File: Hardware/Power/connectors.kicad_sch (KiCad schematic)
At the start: 3 parts, among them J1 Conn_02x23_Odd_Even, J2 Screw_Terminal_01x03, J3 Conn_02x23_Odd_Even

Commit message: schematic update & pcb update
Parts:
- removed J1: Conn_02x23_Odd_Even, PLC_STM_Power:PRT12790, symbol Connector_Generic:Conn_02x23_Odd_Even
- removed J2: Screw_Terminal_01x03, PLC_STM_Power:TBC05031GG, symbol Connector:Screw_Terminal_01x03
- added J1: POWER, PLC_STM:1725656, symbol Connector:Screw_Terminal_01x02
- added J2: NUCLEO LEFT, PLC_STM_Power:PRT12790, symbol Connector_Generic:Conn_02x23_Odd_Even
- J3: value Conn_02x23_Odd_Even -> NUCLEO RIGHT
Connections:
- net +24V: now also J1.2 (Pin_2)
- net GND: now also J3.27 (Pin_27), J3.39 (Pin_39), J3.8 (Pin_8), J1.1 (Pin_1), J2.11 (Pin_11), J2.13 (Pin_13), J2.30 (Pin_30), J2.39 (Pin_39)
- net UART6_TX: now reaches J3.1 (Pin_1)
- net UART6_TX: now also J3.11 (Pin_11), J3.40 (Pin_40)
- net AO1: now reaches J3.10 (Pin_10)
- net ANALOG_IN6: now reaches J3.12 (Pin_12)
- net CAN2_RX: now reaches J3.13 (Pin_13)
- net CAN2_RX: now also J3.7 (Pin_7)
- net ANALOG_IN7: now reaches J3.14 (Pin_14)
- net AI0: now reaches J3.17 (Pin_17)
- net CAN1_RX: now reaches J3.2 (Pin_2)
- net CAN1_RX: now also J2.41 (Pin_41)
- net AVDD: now reaches J3.23 (Pin_23)
- net AVDD: now also J3.6 (Pin_6)
- net AGND: now reaches J3.25 (Pin_25)
- net CAN1_TX: now reaches J3.4 (Pin_4)
- net CAN1_TX: now also J2.43 (Pin_43)
- net UART6_RX: now reaches J3.42 (Pin_42)
- net UART5_TX: now reaches J3.44 (Pin_44)
- net UART5_TX: now also J2.10 (Pin_10)
- net UART5_RX: now reaches J3.46 (Pin_46)
- net UART5_RX: now also J2.12 (Pin_12)
- net CAN2_TX: now reaches J3.5 (Pin_5)
- new net 3V3: J2.7 (Pin_7)
- new net 5V: J2.9 (Pin_9)
- new net ANALOG_IN10: J2.21 (Pin_21)
- new net ANALOG_IN13: J2.23 (Pin_23)
- new net ANALOG_IN3: J2.19 (Pin_19)
- new net ANALOG_IN3/15: J2.27 (Pin_27)
- new net ANALOG_IN3/5: J2.42 (Pin_42)
- new net ANALOG_IN3/6: J2.40 (Pin_40)
- new net ANALOG_IN3/7: J2.44 (Pin_44)
- new net ANALOG_IN3/8: J2.29 (Pin_29)
- new net ANALOG_IN3/9: J2.25 (Pin_25)
- new net UART2_RX: J2.22 (Pin_22)
- new net UART2_TX: J2.24 (Pin_24)
- new net UART4_RX: J2.8 (Pin_8)
- new net UART4_TX: J2.6 (Pin_6)
- new net VIN: J2.15 (Pin_15)
- no-connect marks 1 -> 51
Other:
- moved on the sheet: J3

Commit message: schematic update & pcb update
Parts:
- J2, J3: footprint PLC_STM_Power:PRT12790 -> PLC_STM:PRT12790
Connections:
- net VIN is gone; now on net +5V: J2.15 (Pin_15)
- net +15V: now reaches J3.21 (Pin_21)
- net -15V: now reaches J2.18 (Pin_18)
- net 3V3 renamed +3V3
- net 5V renamed +5V
- net AI0 renamed AO_0
- net ANALOG_IN10: no longer names the net of J2.21 (Pin_21)
- net ANALOG_IN13: no longer names the net of J2.23 (Pin_23)
- net ANALOG_IN3: no longer names the net of J2.19 (Pin_19)
- net ANALOG_IN3/15: no longer names the net of J2.27 (Pin_27)
- net ANALOG_IN3/5: no longer names the net of J2.42 (Pin_42)
- net ANALOG_IN3/6: no longer names the net of J2.40 (Pin_40)
- net ANALOG_IN3/7: no longer names the net of J2.44 (Pin_44)
- net ANALOG_IN3/8: no longer names the net of J2.29 (Pin_29)
- net ANALOG_IN3/9: no longer names the net of J2.25 (Pin_25)
- net AO1 renamed AO_1
- no-connect marks 51 -> 56

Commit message: digital output & power finished
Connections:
- net UART2_RX is gone; now on net GND: J2.22 (Pin_22)
- net +15V: now also J2.10 (Pin_10); no longer J3.21 (Pin_21)
- net +24V: now also J2.29 (Pin_29); no longer J1.2 (Pin_2)
- net +3V3: now also J2.25 (Pin_25); no longer J2.7 (Pin_7)
- net +5V: now also J2.27 (Pin_27); no longer J2.15 (Pin_15), J2.9 (Pin_9)
- net -15V: now also J2.26 (Pin_26); no longer J2.18 (Pin_18)
- net GND: now also J2.19 (Pin_19), J2.20 (Pin_20), J3.20 (Pin_20); no longer J2.11 (Pin_11), J2.13 (Pin_13), J2.30 (Pin_30), J2.39 (Pin_39), J3.27 (Pin_27), J3.8 (Pin_8)
- net AGND: no longer names the net of J3.25 (Pin_25)
- net ANALOG_IN6: no longer names the net of J3.12 (Pin_12)
- net ANALOG_IN7: no longer names the net of J3.14 (Pin_14)
- net AO_0: no longer names the net of J3.17 (Pin_17)
- net AO_1: no longer names the net of J3.10 (Pin_10)
- net AVDD: no longer names the net of J3.23 (Pin_23)
- net AVDD: no longer J3.6 (Pin_6)
- net CAN1_RX: no longer names the net of J3.2 (Pin_2)
- net CAN1_RX: no longer J2.41 (Pin_41)
- net CAN1_TX: no longer names the net of J3.4 (Pin_4)
- net CAN1_TX: no longer J2.43 (Pin_43)
- net CAN2_RX: no longer names the net of J3.13 (Pin_13)
- net CAN2_RX: no longer J3.7 (Pin_7)
- net CAN2_TX: no longer names the net of J3.5 (Pin_5)
- net UART2_TX: no longer names the net of J2.24 (Pin_24)
- net UART4_RX: no longer names the net of J2.8 (Pin_8)
- net UART4_TX: no longer names the net of J2.6 (Pin_6)
- net UART5_RX: no longer names the net of J3.46 (Pin_46)
- net UART5_RX: no longer J2.12 (Pin_12)
- net UART5_TX: no longer names the net of J3.44 (Pin_44)
- net UART5_TX: no longer J2.10 (Pin_10)
- net UART6_RX: no longer names the net of J3.42 (Pin_42)
- removed net UART6_TX: J3.1 (Pin_1), J3.11 (Pin_11), J3.40 (Pin_40)
- new net VCC: J1.2 (Pin_2)
- no-connect marks 56 -> 82

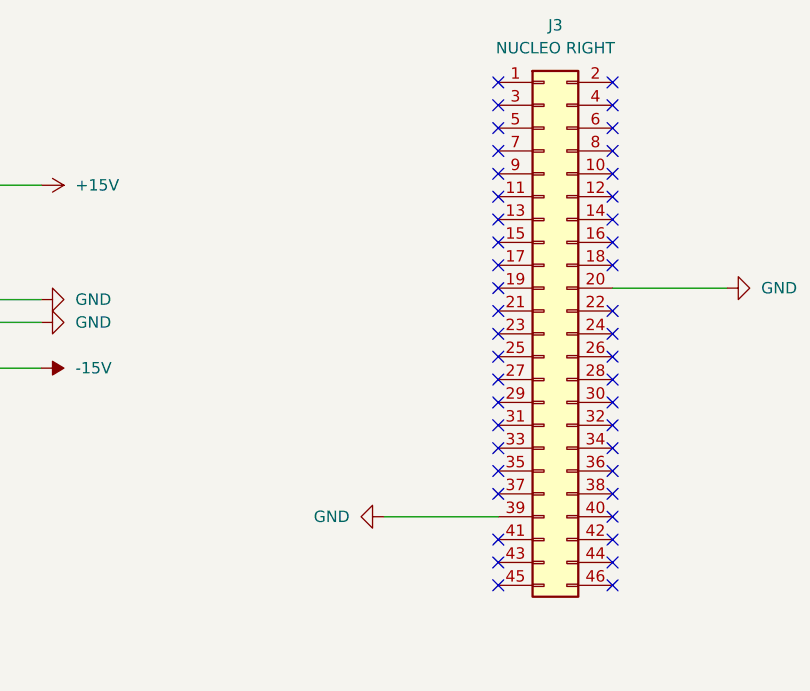
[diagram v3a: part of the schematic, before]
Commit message: analog & can finished
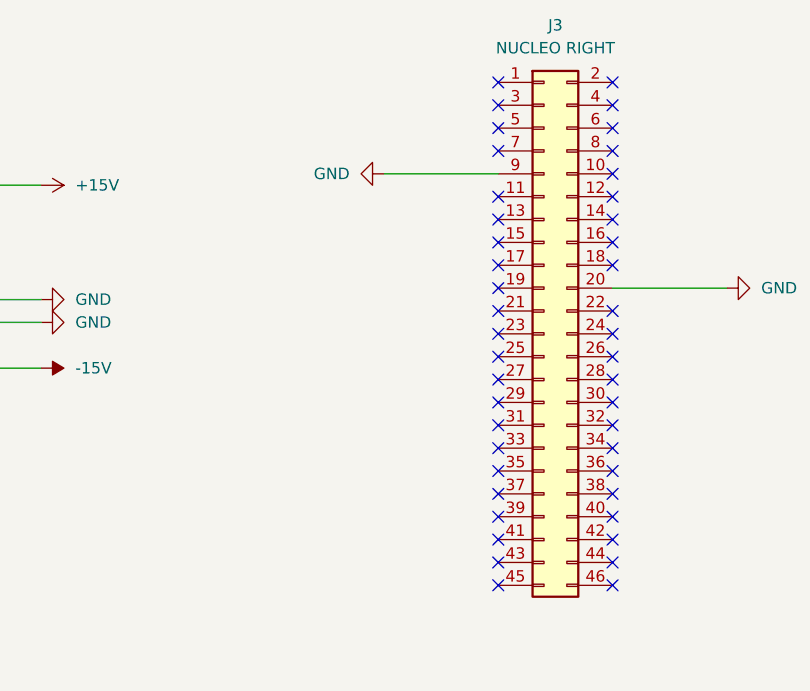
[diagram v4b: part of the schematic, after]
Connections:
- net GND: now also J3.9 (Pin_9); no longer J3.39 (Pin_39)
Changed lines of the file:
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@@
-	)
-	(no_connect
-		(at 217.17 78.74)
 	)
 	(no_connect
@@
 	)
 	(no_connect
+		(at 217.17 116.84)
+	)
+	(no_connect
 		(at 153.67 115.57)
 	)
@@
 	(wire
 		(pts
-			(xy 217.17 116.84) (xy 204.47 116.84)
+			(xy 217.17 78.74) (xy 204.47 78.74)
 		)
 		(stroke
@@
 	(symbol
 		(lib_id "power:GND")
-		(at 204.47 116.84 270)
+		(at 204.47 78.74 270)
 		(mirror x)
 		(unit 1)
@@
 		(fields_autoplaced yes)
 		(property "Reference" "#PWR025"
-			(at 198.12 116.84 0)
+			(at 198.12 78.74 0)
 			(effects
 				(font
@@
 		)
 		(property "Value" "GND"
-			(at 200.66 116.8399 90)
+			(at 200.66 78.7399 90)
 			(effects
 				(font
@@
 		)
 		(property "Footprint" ""
-			(at 204.47 116.84 0)
+			(at 204.47 78.74 0)
 			(effects
 				(font
@@
 		)
 		(property "Datasheet" ""
-			(at 204.47 116.84 0)
+			(at 204.47 78.74 0)
 			(effects
 				(font
@@
 		)
 		(property "Description" "Power symbol creates a global label with name \"GND\" , ground"
-			(at 204.47 116.84 0)
-			(effects
-				(font
+			(at 204.47 78.74 0)
+			(effects
+				(font
